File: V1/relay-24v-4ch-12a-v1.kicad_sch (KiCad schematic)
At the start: 24 parts, among them J1 DB141V-2.54-2P, J2 DB141V-2.54-4P, J3 DB142V-5.08-4P, J4 DB142V-5.08-4P, K1 G5PZ-1A, K2 G5PZ-1A, K3 G5PZ-1A, K4 G5PZ-1A

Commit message: Replaced terminal blocks
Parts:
- J1: value DB141V-2.54-2P -> +24V; footprint Tales:TerminalBlock_Dibo_DB141V-2.54-2P_1x02_P2.54mm_Vertical -> Tales:TerminalBlock_Wago_250-202_1x02_P3.5mm_45Degree; LCSC Part # C2898744 -> C2765061; Mfr DORABO -> Wago; Mfr PN DB141V-2.54-2P-GN -> 250-202; Vendor PN C2898744 -> C2765061
- J2: value DB141V-2.54-4P -> INPUTS; footprint Tales:TerminalBlock_Dibo_DB141V-2.54-4P_1x04_P2.54mm_Vertical -> Tales:TerminalBlock_Wago_250-204_1x04_P3.5mm_45Degree; LCSC Part # C2898746 -> C2765063; Mfr DORABO -> Wago; Mfr PN DB141V-2.54-4P-GN -> 250-204; Vendor PN C2898746 -> C2765063

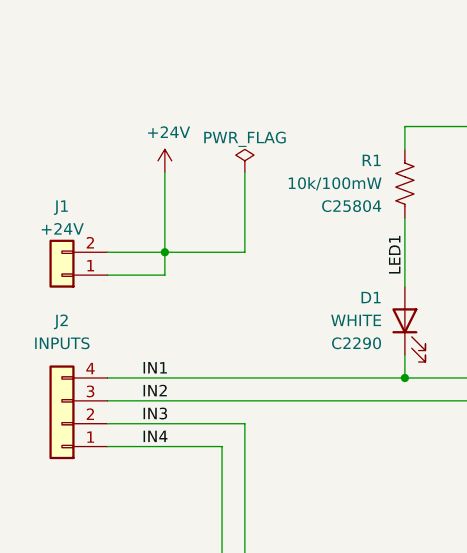
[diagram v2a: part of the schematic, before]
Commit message: Replaced input terminal blocks for 3.5mm pitch.
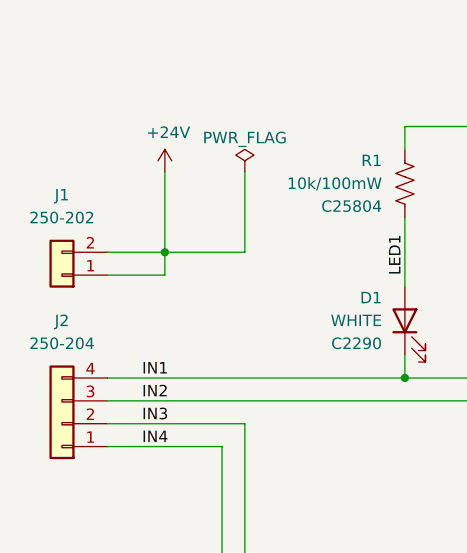
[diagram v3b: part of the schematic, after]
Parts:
- J1: value +24V -> 250-202
- J2: value INPUTS -> 250-204
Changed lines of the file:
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@@
 		(in_pos_files yes)
 		(dnp no)
+		(fields_autoplaced yes)
 		(property "Reference" "J2"
 			(at 35.56 80.01 0)
@@
 			)
 		)
-		(property "Value" "INPUTS"
+		(property "Value" "250-204"
 			(at 35.56 82.55 0)
 			(show_name no)
@@
 		(in_pos_files yes)
 		(dnp no)
+		(fields_autoplaced yes)
 		(property "Reference" "J1"
-			(at 35.56 67.31 0)
-			(show_name no)
-			(do_not_autoplace no)
-			(effects
-				(font
-					(size 1.27 1.27)
-				)
-			)
-		)
-		(property "Value" "+24V"
-			(at 35.56 69.85 0)
-			(show_name no)
-			(do_not_autoplace no)
+			(at 35.56 66.04 0)
+			(show_name no)
+			(do_not_autoplace no)
+			(effects
+				(font
+					(size 1.27 1.27)
+				)
+			)
+		)
+		(property "Value" "250-202"
+			(at 35.56 68.58 0)
+			(show_name no)
+			(do_not_autoplace no)
